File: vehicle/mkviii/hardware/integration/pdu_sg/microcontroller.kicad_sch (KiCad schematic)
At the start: 69 parts, among them J1 J_Programming_Pin_Header, U1 STM32G441KBT6, U11 CA56-12SEKWA, U12 MAX7221xNG, U13 MCP23S17-E_SO, U2 MCP2561-E_SN, U20 ADC1283, Y1 X_16MHz_18pF

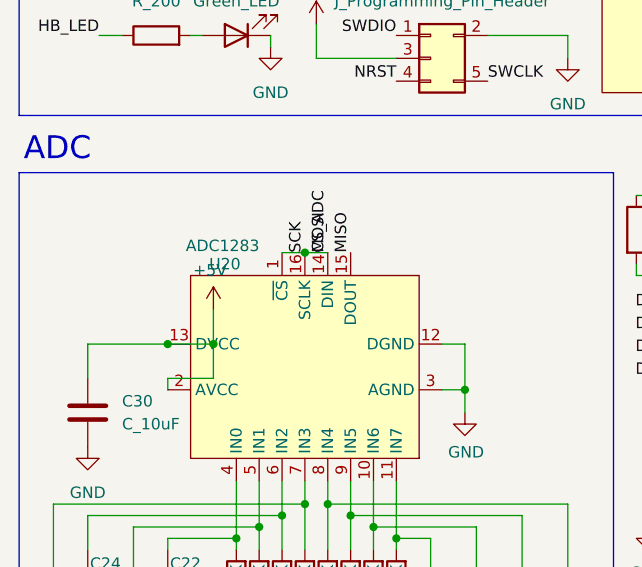
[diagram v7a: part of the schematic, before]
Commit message: fix footprints
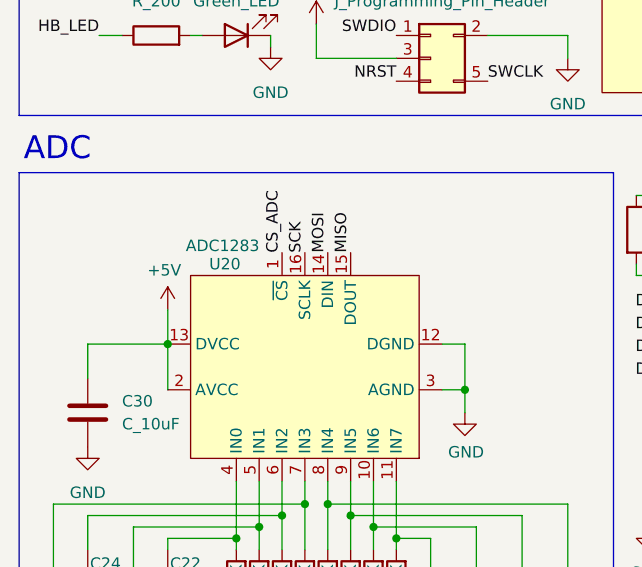
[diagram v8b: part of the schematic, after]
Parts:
- C1, C2, C3, C30, C31, C4, C5, C6, C7, C8, C9: footprint OEM:C_0603_1608Metric -> Capacitor_SMD:C_0603_1608Metric
- R18, R20, R45, R54, R55, R56, R57, R58, R59: footprint OEM:R_0603 -> Resistor_SMD:R_0603_1608Metric
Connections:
- net CS_ADC: no longer U1.26 ((TIM3_ETR/SPI1_SCK/TIM4_ETR/TIM2_CH2/GPIO_EXTI3)PB3), U1.28 ((TIM17_CH1/SPI1_MOSI/TIM3_CH2/TIM16_BKIN/GPIO_EXTI5)PB5), U12.1 (DIN), U12.13 (CLK), U13.12 (SCK), U13.13 (SI), U20.14 (DIN), U20.16 (SCLK)
- new net MOSI: U1.28 ((TIM17_CH1/SPI1_MOSI/TIM3_CH2/TIM16_BKIN/GPIO_EXTI5)PB5), U12.1 (DIN), U13.13 (SI), U20.14 (DIN)
- new net SCK: U1.26 ((TIM3_ETR/SPI1_SCK/TIM4_ETR/TIM2_CH2/GPIO_EXTI3)PB3), U12.13 (CLK), U13.12 (SCK), U20.16 (SCLK)
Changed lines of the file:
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@@
 	)
 	(junction
-		(at 45.72 127)
-		(diameter 0)
-		(color 0 0 0 0)
-	)
-	(junction
 		(at 43.18 156.21)
 		(diameter 0)
@@
 	)
 	(junction
-		(at 35.56 137.16)
-		(diameter 0)
-		(color 0 0 0 0)
-	)
-	(junction
 		(at 72.39 40.64)
 		(diameter 0)
@@
 	(wire
 		(pts
-			(xy 43.18 127) (xy 45.72 127)
-		)
-		(stroke
-			(width 0)
-			(type default)
-		)
-	)
-	(wire
-		(pts
 			(xy 26.67 180.34) (xy 26.67 157.48)
 		)
@@
 	(wire
 		(pts
-			(xy 35.56 133.35) (xy 35.56 137.16)
+			(xy 30.48 133.35) (xy 30.48 137.16)
 		)
 		(stroke
@@
 	(wire
 		(pts
-			(xy 30.48 140.97) (xy 30.48 142.24)
+			(xy 30.48 137.16) (xy 30.48 142.24)
 		)
 		(stroke
@@
 	(wire
 		(pts
-			(xy 35.56 140.97) (xy 35.56 137.16)
-		)
-		(stroke
-			(width 0)
-			(type default)
-		)
-	)
-	(wire
-		(pts
 			(xy 46.99 66.04) (xy 46.99 64.77)
 		)
@@
 	(wire
 		(pts
-			(xy 30.48 140.97) (xy 35.56 140.97)
-		)
-		(stroke
-			(width 0)
-			(type default)
-		)
-	)
-	(wire
-		(pts
 			(xy 109.22 137.16) (xy 107.95 137.16)
 		)
@@
 	(wire
 		(pts
-			(xy 45.72 127) (xy 48.26 127)
-		)
-		(stroke
-			(width 0)
-			(type default)
-		)
-	)
-	(wire
-		(pts
 			(xy 255.27 64.77) (xy 255.27 66.04)
 		)
@@
 	(wire
 		(pts
-			(xy 30.48 137.16) (xy 35.56 137.16)
-		)
-		(stroke
-			(width 0)
-			(type default)
-		)
-	)
-	(wire
-		(pts
 			(xy 256.54 96.52) (xy 252.73 96.52)
 		)
@@
 	)
 	(label "CS_ADC"
-		(at 48.26 127 90)
+		(at 43.18 127 90)
 		(effects
 			(font
@@
 			)
 		)
-		(property "Footprint" "OEM:R_0603"
+		(property "Footprint" "Resistor_SMD:R_0603_1608Metric"
 			(at 44.958 163.83 90)
 			(hide yes)
@@
 			)
 		)
-		(property "Footprint" "OEM:R_0603"
+		(property "Footprint" "Resistor_SMD:R_0603_1608Metric"
 			(at 32.512 176.53 90)
 			(hide yes)
@@
 			)
 		)
-		(property "Footprint" "OEM:C_0603_1608Metric"
+		(property "Footprint" "Capacitor_SMD:C_0603_1608Metric"
 			(at 20.0152 53.34 0)
 			(hide yes)
@@
 			)
 		)
-		(property "Footprint" "OEM:C_0603_1608Metric"
+		(property "Footprint" "Capacitor_SMD:C_0603_1608Metric"
 			(at 29.5148 80.01 0)
 			(hide yes)
@@
 			)
 		)
-		(property "Footprint" "OEM:C_0603_1608Metric"
+		(property "Footprint" "Capacitor_SMD:C_0603_1608Metric"
 			(at 159.7152 34.29 0)
 			(hide yes)
@@
 			)
 		)
-		(property "Footprint" "OEM:R_0603"
+		(property "Footprint" "Resistor_SMD:R_0603_1608Metric"
 			(at 57.658 163.83 90)
 			(hide yes)
@@
 	(symbol
 		(lib_id "power:+5V")
-		(at 35.56 133.35 0)
+		(at 30.48 133.35 0)
 		(mirror y)
 		(unit 1)
@@
 		(dnp no)
 		(property "Reference" "#PWR075"
-			(at 35.56 137.16 0)
+			(at 30.48 137.16 0)
 			(hide yes)
 			(show_name no)
@@
 		)
 		(property "Value" "+5V"
-			(at 35.179 128.9558 0)
+			(at 30.099 128.9558 0)
 			(show_name no)
 			(do_not_autoplace no)
@@
 		)
 		(property "Footprint" ""
-			(at 35.56 133.35 0)
+			(at 30.48 133.35 0)
 			(hide yes)
 			(show_name no)
@@
 		)
 		(property "Datasheet" ""
-			(at 35.56 133.35 0)
+			(at 30.48 133.35 0)
 			(hide yes)
 			(show_name no)
@@
 		)
 		(property "Description" "Power symbol creates a global label with name \"+5V\""
-			(at 35.56 133.35 0)
+			(at 30.48 133.35 0)
 			(hide yes)
 			(show_name no)
@@
 			)
 		)
-		(property "Footprint" "OEM:R_0603"
+		(property "Footprint" "Resistor_SMD:R_0603_1608Metric"
 			(at 47.498 163.83 90)
 			(hide yes)
@@
 			)
 		)
-		(property "Footprint" "OEM:C_0603_1608Metric"
+		(property "Footprint" "Capacitor_SMD:C_0603_1608Metric"
 			(at 25.0952 35.56 0)
 			(hide yes)
@@
 			)
 		)
-		(property "Footprint" "OEM:R_0603"
+		(property "Footprint" "Resistor_SMD:R_0603_1608Metric"
 			(at 55.118 163.83 90)
 			(hide yes)
@@
 			)
 		)
-		(property "Footprint" "OEM:C_0603_1608Metric"
+		(property "Footprint" "Capacitor_SMD:C_0603_1608Metric"
 			(at 41.6052 35.56 0)
 			(hide yes)
@@
 			)
 		)
-		(property "Footprint" "OEM:R_0603"
+		(property "Footprint" "Resistor_SMD:R_0603_1608Metric"
 			(at 39.878 163.83 90)
 			(hide yes)
@@
 			)
 		)
-		(property "Footprint" "OEM:C_0603_1608Metric"
+		(property "Footprint" "Capacitor_SMD:C_0603_1608Metric"
 			(at 22.5552 148.59 0)
 			(hide yes)
@@
 			)
 		)
-		(property "Footprint" "OEM:R_0603"
+		(property "Footprint" "Resistor_SMD:R_0603_1608Metric"
 			(at 42.418 163.83 90)
 			(hide yes)
@@
 			)
 		)
-		(property "Footprint" "OEM:C_0603_1608Metric"
+		(property "Footprint" "Capacitor_SMD:C_0603_1608Metric"
 			(at 57.4548 80.01 0)
 			(hide yes)
@@
 			)
 		)
-		(property "Footprint" "OEM:R_0603"
+		(property "Footprint" "Resistor_SMD:R_0603_1608Metric"
 			(at 50.038 163.83 90)
 			(hide yes)
@@
 			)
 		)
-		(property "Footprint" "OEM:C_0603_1608Metric"
+		(property "Footprint" "Capacitor_SMD:C_0603_1608Metric"
 			(at 41.6052 53.34 0)
 			(hide yes)
@@
 			)
 		)
-		(property "Footprint" "OEM:R_0603"
+		(property "Footprint" "Resistor_SMD:R_0603_1608Metric"
 			(at 52.578 163.83 90)
 			(hide yes)
@@
 			)
 		)
-		(property "Footprint" "OEM:C_0603_1608Metric"
+		(property "Footprint" "Capacitor_SMD:C_0603_1608Metric"
 			(at 192.0748 68.58 0)
 			(hide yes)
@@
 			)
 		)
-		(property "Footprint" "OEM:C_0603_1608Metric"
+		(property "Footprint" "Capacitor_SMD:C_0603_1608Metric"
 			(at 118.4148 189.23 0)
 			(hide yes)
@@
 			)
 		)
-		(property "Footprint" "OEM:C_0603_1608Metric"
+		(property "Footprint" "Capacitor_SMD:C_0603_1608Metric"
 			(at 58.1152 35.56 0)
 			(hide yes)
